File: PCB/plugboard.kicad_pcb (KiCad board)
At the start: 2 copper layers, 100 x 100 mm, 96 parts, among them J1 1/4" Jack, J10 1/4" Jack, J11 Conn_01x19_Male_0, J2 1/4" Jack, J3 1/4" Jack, J4 1/4" Jack, J5 1/4" Jack, J6 1/4" Jack, J7 Conn_01x19_Male_0, J8 1/4" Jack, J9 1/4" Jack, P1 CONN_02X03, P2 CONN_02X03, U1 ADG732

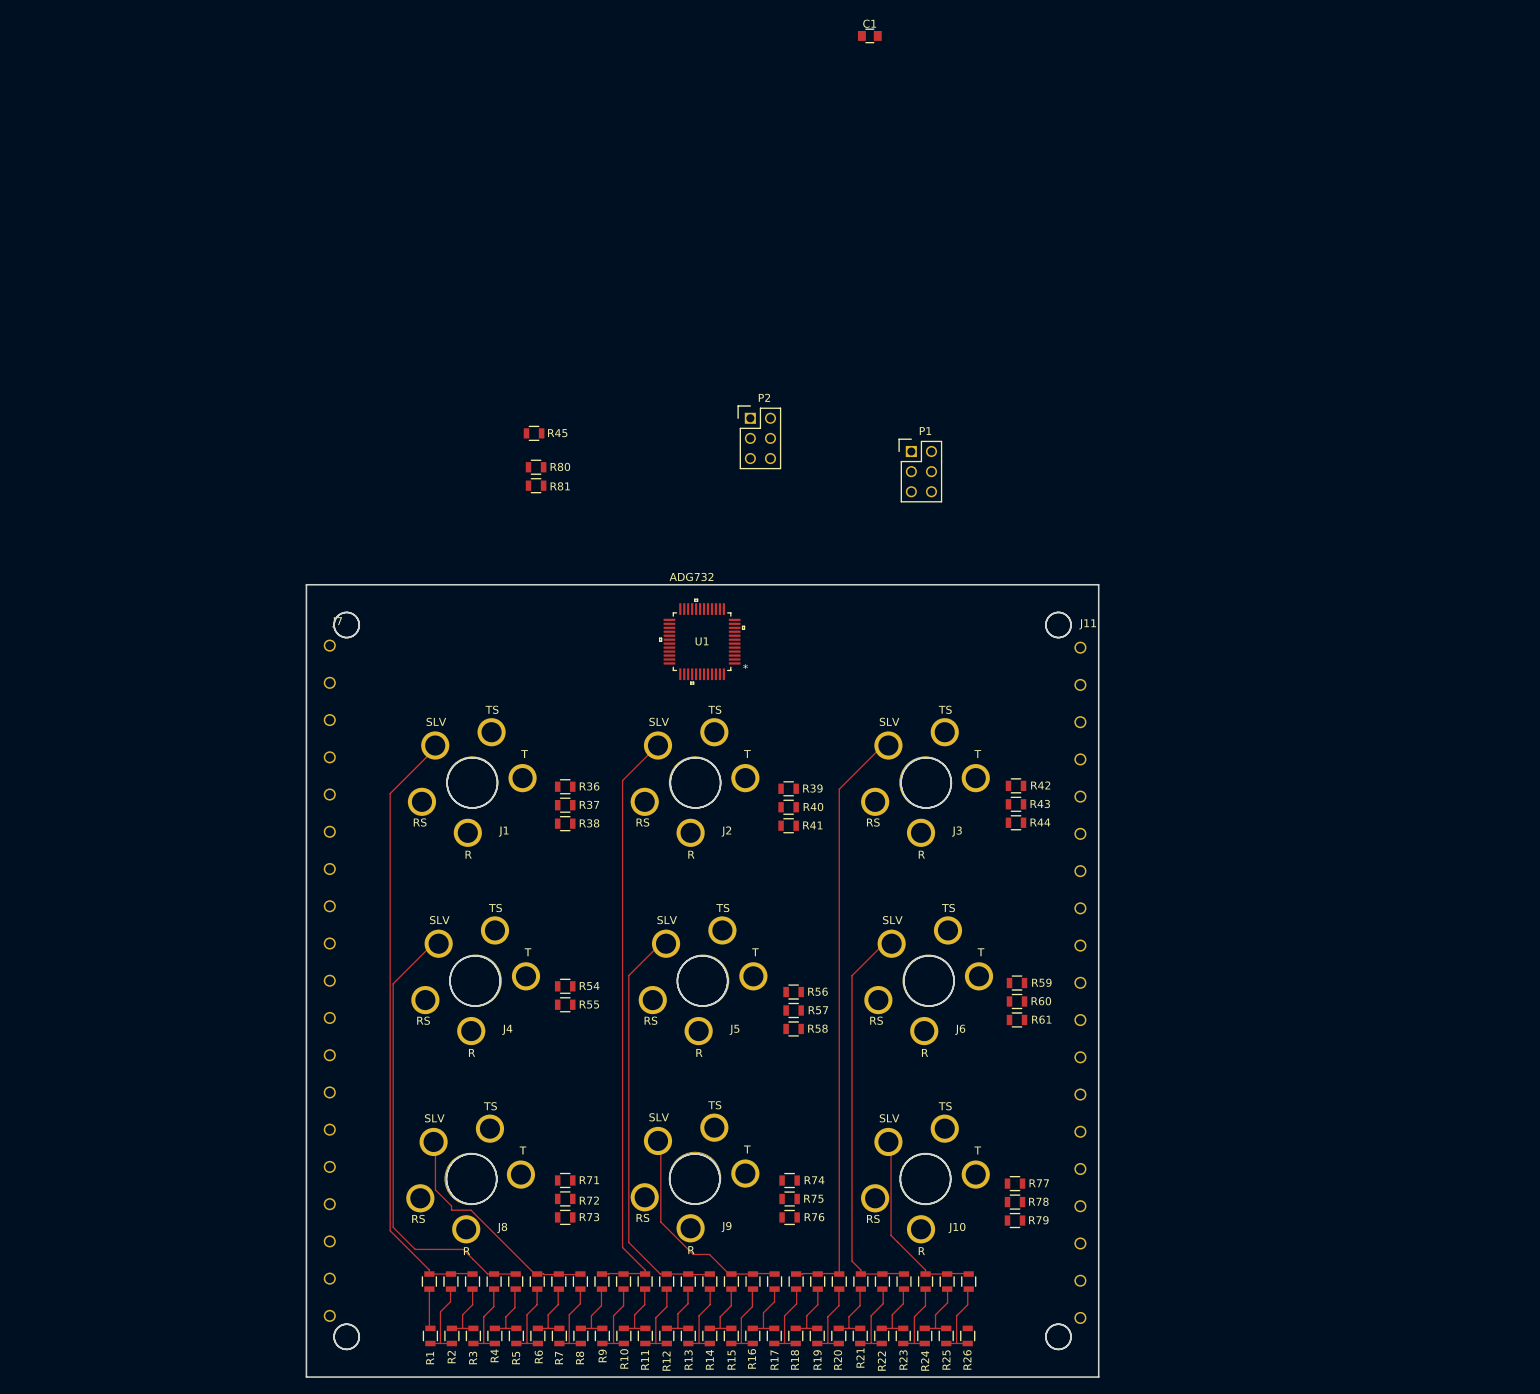
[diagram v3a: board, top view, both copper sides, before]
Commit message: Layout work
It's working!
I did a few optimization changes to make layout smoother.
Changed around the netlist essentially
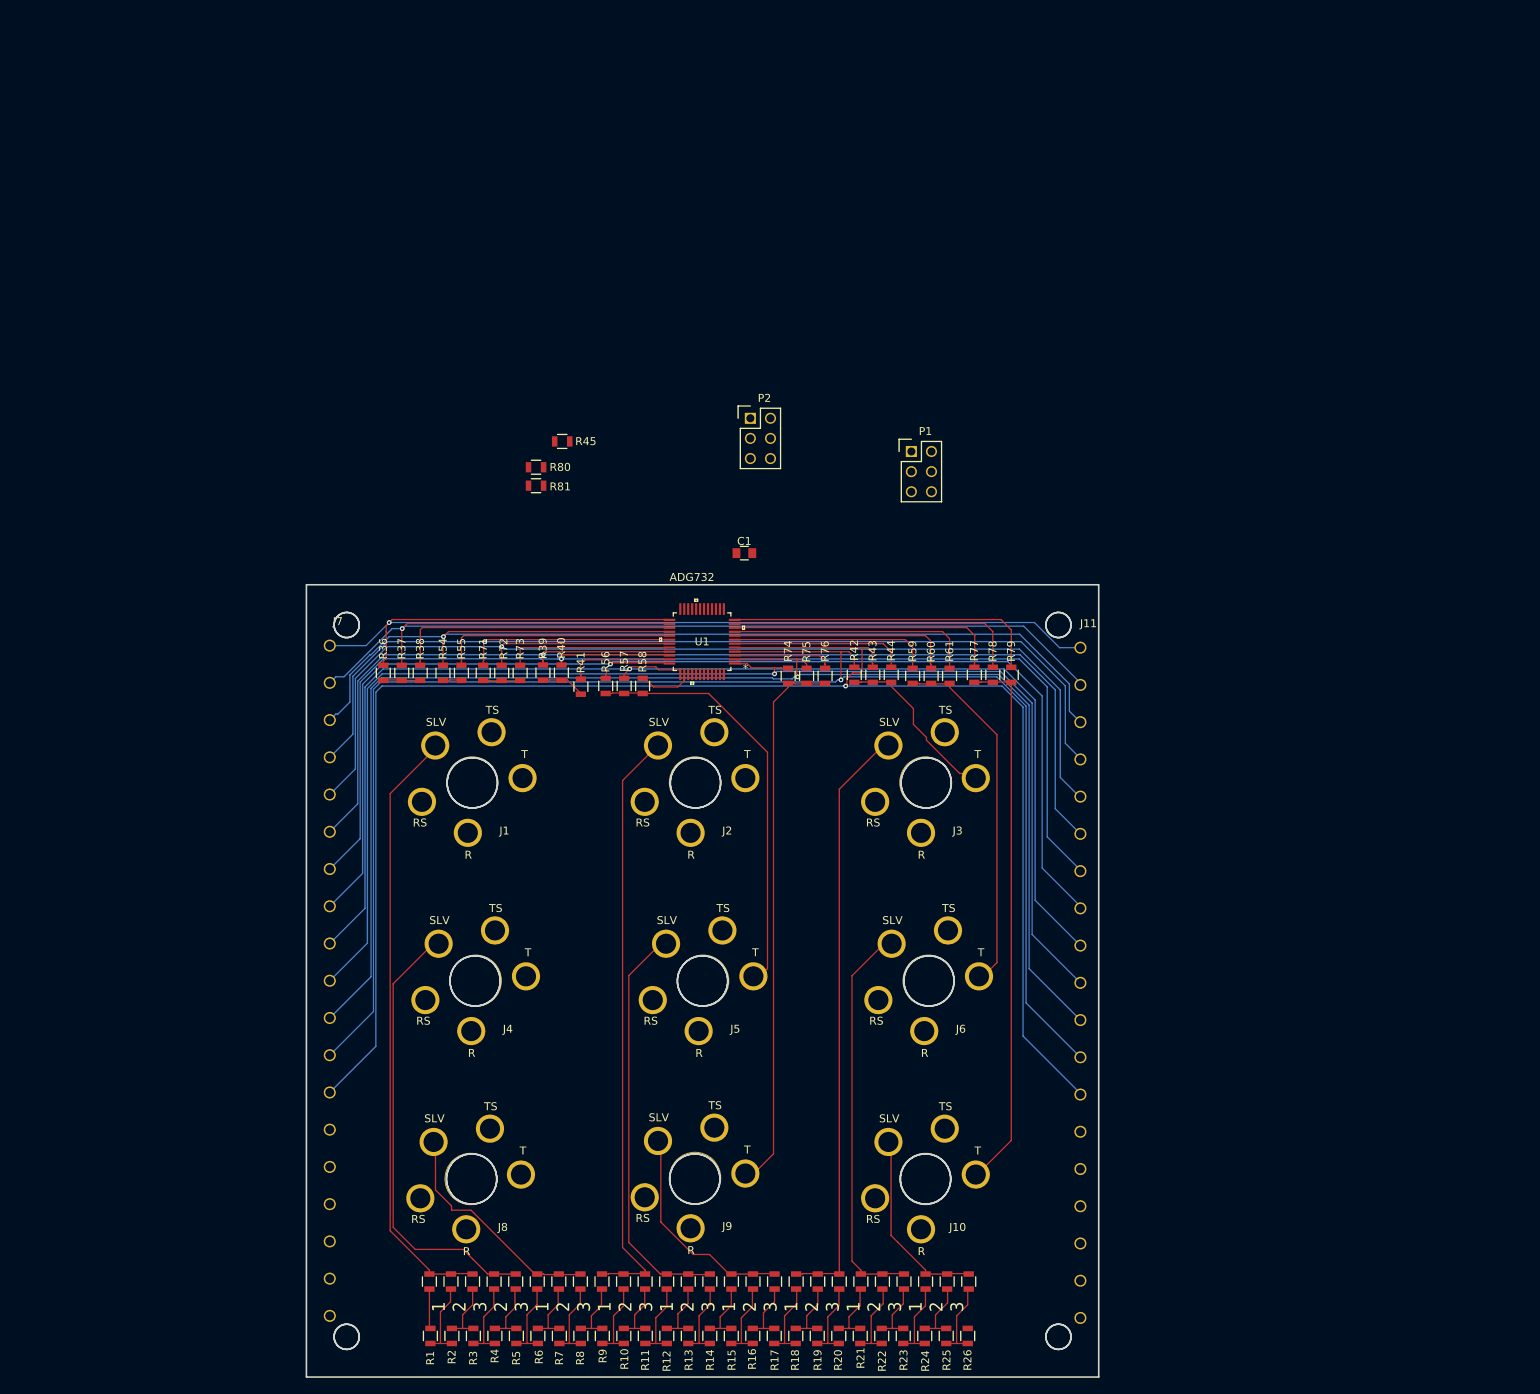
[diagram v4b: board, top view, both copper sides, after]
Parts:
- moved R73 69.0 mm to (116.7, 92.3), turned to 90 degrees
- moved R79 68.9 mm to (178.7, 92.6), turned to 90 degrees
- moved R76 68.5 mm to (155.2, 92.7), turned to 90 degrees
- moved C1 67.2 mm to (145.0, 77.2)
- moved R72 66.9 mm to (114.4, 92.3), turned to 90 degrees
- moved R78 66.6 mm to (176.4, 92.6), turned to 90 degrees
- moved R75 66.1 mm to (152.9, 92.7), turned to 90 degrees
- moved R71 64.9 mm to (112.1, 92.3), turned to 90 degrees
- moved R77 64.4 mm to (174.1, 92.6), turned to 90 degrees
- moved R74 63.7 mm to (150.6, 92.7), turned to 90 degrees
- moved R58 47.3 mm to (132.2, 94.0), turned to 90 degrees
- moved R57 46.2 mm to (129.9, 94.0), turned to 90 degrees
- moved R56 45.3 mm to (127.5, 94.0), turned to 90 degrees
- moved R61 44.3 mm to (170.9, 92.7), turned to 90 degrees
- moved R55 43.9 mm to (109.3, 92.3), turned to 90 degrees
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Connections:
- J11 pad 10: /SD -> /SY
- J11 pad 11: /SC -> /SV
- J11 pad 12: /ST -> /SE
- J11 pad 13: /SF -> /SZ
- J11 pad 14: /SV -> /SS
- J11 pad 15: /SZ -> /SG
- J11 pad 16: /SG -> /SX
- J11 pad 2: /SP -> /SR
- J11 pad 3: /SW -> /SD
- J11 pad 4: /SA -> /SP
- J11 pad 5: /SY -> /SC
- J11 pad 6: /SE -> /SW
- J11 pad 7: /SS -> /ST
- J11 pad 8: /SX -> /SA
- J11 pad 9: /SR -> /SF
- J7 pad 10: /SD -> /SY
- J7 pad 11: /SC -> /SV
- J7 pad 12: /ST -> /SE
- J7 pad 13: /SF -> /SZ
- J7 pad 14: /SV -> /SS
- J7 pad 15: /SZ -> /SG
- J7 pad 16: /SG -> /SX
- J7 pad 2: /SP -> /SR
- J7 pad 3: /SW -> /SD
- J7 pad 4: /SA -> /SP
- J7 pad 5: /SY -> /SC
- J7 pad 6: /SE -> /SW
- J7 pad 7: /SS -> /ST
- J7 pad 8: /SX -> /SA
- J7 pad 9: /SR -> /SF
- U1 pad 1: /SS -> /SY
- U1 pad 10: Net-(U1-Pad10) -> /SX
- U1 pad 11: Net-(U1-Pad11) -> /SB
- U1 pad 12: Net-(U1-Pad12) -> /SL
- U1 pad 2: /SG -> /SV
- U1 pad 3: /SK -> /SM
- U1 pad 39: /SY -> Net-(U1-Pad39)
- U1 pad 4: /SX -> /SE
- U1 pad 40: /SV -> Net-(U1-Pad40)
- U1 pad 45: /SM -> Net-(U1-Pad45)
- U1 pad 46: /SE -> Net-(U1-Pad46)
- U1 pad 47: /SZ -> Net-(U1-Pad47)
- U1 pad 48: /SO -> Net-(U1-Pad48)
- U1 pad 5: /SB -> /SZ
- U1 pad 6: /SL -> /SO
- U1 pad 7: Net-(U1-Pad7) -> /SS
- U1 pad 8: Net-(U1-Pad8) -> /SG
- U1 pad 9: Net-(U1-Pad9) -> /SK
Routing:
- net /SZ: track 0.00 -> 213.1 mm, vias 0 -> 1
- net /SE: track 0.00 -> 199.9 mm, vias 0 -> 1
- net /SV: track 0.00 -> 183.5 mm, vias 0 -> 1
- net /SY: track 0.00 -> 170.3 mm, vias 0 -> 1
- net /SF: track 0.00 -> 162.6 mm, vias 0 -> 1
- net /SA: track 0.00 -> 156.3 mm, vias 0 -> 1
- net /ST: track 0.00 -> 154.1 mm, vias 0 -> 1
- net /SW: track 0.00 -> 148.3 mm, vias 0 -> 1
- net /SC: track 0.00 -> 147.1 mm, vias 0 -> 1
- net /SP: track 0.00 -> 141.6 mm, vias 0 -> 1
- net /SD: track 0.00 -> 139.8 mm, vias 0 -> 1
- net /SR: track 0.00 -> 139.1 mm, vias 0 -> 1
- net /SQ: track 0.00 -> 138.3 mm, vias 0 -> 1
- net Net-(J9-Pad3): track 0.00 -> 67.6 mm
- net Net-(J10-Pad3): track 0.00 -> 67.2 mm
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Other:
- board text added: "1 2 3 2 3 1 2 3 1 2 3 1 2 3 1 2 3 1 2 3 1 2 3 1 2 3"

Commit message: Finish first draft layout
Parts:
- P1, P2: moved to B.Cu
- moved P1 66.7 mm to (124.2, 116.3)
- moved R81 55.0 mm to (124.6, 123.4)
- moved R80 55.0 mm to (124.6, 121.1)
- moved P2 50.3 mm to (124.1, 105.5)
- moved R45 34.8 mm to (126.0, 97.7)
- moved C1 25.3 mm to (130.2, 97.7), turned to 270 degrees
- turned U1 to 0 degrees
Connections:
- U1 pad 1: /SY -> /SR
- U1 pad 10: /SX -> /SI
- U1 pad 11: /SB -> /SA
- U1 pad 12: /SL -> /SJ
- U1 pad 2: /SV -> /SU
- U1 pad 25: /SQ -> /SY
- U1 pad 26: /SR -> /SV
- U1 pad 27: /SU -> /SM
- U1 pad 28: /SD -> /SE
- U1 pad 29: /SH -> /SZ
- U1 pad 3: /SM -> /SD
- U1 pad 30: /SP -> /SO
- U1 pad 31: /SC -> /SS
- U1 pad 32: /SN -> /SG
- U1 pad 33: /SW -> /SK
- U1 pad 34: /ST -> /SX
- U1 pad 35: /SI -> /SB
- U1 pad 36: /SA -> /SL
- U1 pad 38: /SJ -> Net-(U1-Pad38)
- U1 pad 4: /SE -> /SH
- U1 pad 48: Net-(U1-Pad48) -> /SQ
- U1 pad 5: /SZ -> /SP
- U1 pad 6: /SO -> /SC
- U1 pad 7: /SS -> /SN
- U1 pad 8: /SG -> /SW
- U1 pad 9: /SK -> /ST
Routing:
- net GND: track 0.00 -> 265.1 mm, vias 0 -> 5
- net VCC: track 4.77 -> 244.6 mm, vias 0 -> 1
- net /SB: track 36.9 -> 269.6 mm, vias 0 -> 1
- net /SX: track 34.2 -> 256.8 mm, vias 0 -> 1
- net /SG: track 27.9 -> 242.1 mm, vias 0 -> 1
- net /SS: track 25.0 -> 228.2 mm, vias 0 -> 1
- net Net-(J8-Pad3): track 4.54 -> 69.1 mm, vias 0 -> 2
- net /~CS: track 0.00 -> 43.9 mm
- net Net-(J4-Pad3): track 1.99 -> 43.7 mm, vias 0 -> 2
- net /~EN: track 0.00 -> 40.4 mm
- net /Dout: track 0.00 -> 29.0 mm, vias 0 -> 1
- net Net-(J2-Pad3): track 5.59 -> 33.0 mm, vias 0 -> 1
- net /A0: track 0.00 -> 26.0 mm
- net /A3: track 0.00 -> 23.5 mm
- net /A1: track 0.00 -> 22.3 mm
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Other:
- board text added: "1 2"
- board text added: "1 2 3"
- board text added: "3"
